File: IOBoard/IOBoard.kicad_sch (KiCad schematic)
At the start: 1 part, among them J1 Conn_02x20_Odd_Even

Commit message: complete schematic for usb hub
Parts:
- added C1, C2, C3: 10uF, symbol Device:C
- added J2, J3, J5: USB_A, symbol Connector:USB_A
- added J4, J6: USB_C_Receptacle_USB2.0_14P, symbol Connector:USB_C_Receptacle_USB2.0_14P
- added R1, R2, R3, R4: 5.1k, symbol Device:R
- added U1: ~, SL2.1A:SOP-16_L10.0-W3.9-P1.27-LS6.0-BL, symbol SL2.1A:SL2.1A
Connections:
- new net: C3.2, U1.13 (VDD33)
- new net: J4.A5 (CC1), R2.1
- new net: J4.A6 (D+), J4.B6 (D+), U1.4 (DP3)
- new net: J4.A7 (D-), J4.B7 (D-), U1.3 (DM3)
- new net: J4.B5 (CC2), R1.1
- new net: J6.A5 (CC1), R4.1
- new net: J3.2 (D-), U1.7 (DM1)
- new net: J3.3 (D+), U1.8 (DP1)
- new net: J6.A6 (D+), J6.B6 (D+), U1.2 (DP4)
- new net: J6.A7 (D-), J6.B7 (D-), U1.1 (DM4)
- new net: J6.B5 (CC2), R3.1
- new net: J2.3 (D+), U1.10 (DP)
- new net: C2.2, U1.14 (VDD18)
- new net: J5.2 (D-), U1.5 (DM2)
- new net: J5.3 (D+), U1.6 (DP2)
- new net: J2.2 (D-), U1.9 (DM)
- new net GND: C1.2, C2.1, C3.1, J2.4 (GND), J2.5 (Shield), J3.4 (GND), J3.5 (Shield), J4.A1 (GND), J4.A12 (GND), J4.B1 (GND), J4.B12 (GND), J4.S1 (SHIELD), J5.4 (GND), J5.5 (Shield), J6.A1 (GND), J6.A12 (GND), J6.B1 (GND), J6.B12 (GND), J6.S1 (SHIELD), R1.2, R2.2, R3.2, R4.2, U1.12 (GND), U1.16 (XIN)
- new net VCC: C1.1, J2.1 (VBUS), J3.1 (VBUS), J4.A4 (VBUS), J4.A9 (VBUS), J4.B4 (VBUS), J4.B9 (VBUS), J5.1 (VBUS), J6.A4 (VBUS), J6.A9 (VBUS), J6.B4 (VBUS), J6.B9 (VBUS), U1.11 (VDD5)
- no-connect marks 0 -> 1

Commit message: feat: complete IOBoard
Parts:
- removed J3, J5: USB_A, symbol Connector:USB_A
- added C4, C5, C6, C7: 10uF, Capacitor_SMD:C_0603_1608Metric, symbol Device:C
- added D1: D, Diode_SMD:D_SOD-323, symbol Device:D
- added J7: Conn_01x03, Connector_PinHeader_2.54mm:PinHeader_1x03_P2.54mm_Vertical, symbol Connector_Generic:Conn_01x03
- added J8: Conn_02x20_Odd_Even, Connector_PinHeader_2.54mm:PinHeader_2x20_P2.54mm_Vertical, symbol Connector_Generic:Conn_02x20_Odd_Even
- added USB1: ~, Components:USB-A-TH_AF-SS-JB17.6, symbol USB:AF SS-JB17.6
- C1, C2, C3: footprint (none) -> Capacitor_SMD:C_0603_1608Metric
- J2: footprint (none) -> Components:USB-A-TH_USB-231-ARY
- J4, J6: footprint (none) -> Components:USB-TYPE-C-SMD_TYPE-C-16P-QTWT
- R1, R2, R3, R4: footprint (none) -> Resistor_SMD:R_0603_1608Metric
- U1: footprint SL2.1A:SOP-16_L10.0-W3.9-P1.27-LS6.0-BL -> Components:SL2.1A
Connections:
- net GND: now also J1.14 (Pin_14), J1.20 (Pin_20), J1.25 (Pin_25), J1.30 (Pin_30), J1.34 (Pin_34), J1.39 (Pin_39), J1.6 (Pin_6), J1.9 (Pin_9), C4.2, C5.2, C6.1, C7.1, J7.3 (Pin_3), J8.14 (Pin_14), J8.20 (Pin_20), J8.25 (Pin_25), J8.30 (Pin_30), J8.34 (Pin_34), J8.39 (Pin_39), J8.6 (Pin_6), J8.9 (Pin_9), USB1.10 (SHELL), USB1.11 (SHELL), USB1.12 (SHELL), USB1.4 (GND), USB1.8 (GND), USB1.9 (SHELL)
- net VCC: now also J1.2 (Pin_2), J1.4 (Pin_4), C4.1, C5.1, C6.2, C7.2, D1.1 (K), J7.2 (Pin_2), J8.2 (Pin_2), J8.4 (Pin_4), USB1.1 (VCC), USB1.5 (VCC); no longer C1.1, J2.1 (VBUS)
- net at U1.7 (DM1): now also USB1.2 (D-)
- net at U1.8 (DP1): now also USB1.3 (D+)
- net +3.3V: now reaches J1.1 (Pin_1)
- net +3.3V: now also J1.17 (Pin_17), J8.1 (Pin_1), J8.17 (Pin_17)
- net GPIO_16: now reaches J1.10 (Pin_10)
- net GPIO_16: now also J8.10 (Pin_10)
- net GPIO_0: now reaches J1.11 (Pin_11)
- net GPIO_0: now also J8.11 (Pin_11)
- net GPIO_1: now reaches J1.12 (Pin_12)
- net GPIO_1: now also J8.12 (Pin_12)
- net GPIO_2: now reaches J1.13 (Pin_13)
- net GPIO_2: now also J8.13 (Pin_13)
- net GPIO_3: now reaches J1.15 (Pin_15)
- net GPIO_3: now also J8.15 (Pin_15)
- net GPIO_4: now reaches J1.16 (Pin_16)
- net GPIO_4: now also J8.16 (Pin_16)
- net GPIO_5: now reaches J1.18 (Pin_18)
- net GPIO_5: now also J8.18 (Pin_18)
- net GPIO_12: now reaches J1.19 (Pin_19)
- net GPIO_12: now also J8.19 (Pin_19)
- net GPIO_13: now reaches J1.21 (Pin_21)
- net GPIO_13: now also J8.21 (Pin_21)
- net GPIO_6: now reaches J1.22 (Pin_22)
- net GPIO_6: now also J8.22 (Pin_22)
- net GPIO_14: now reaches J1.23 (Pin_23)
- net GPIO_14: now also J8.23 (Pin_23)
- net GPIO_10: now reaches J1.24 (Pin_24)
- net GPIO_10: now also J8.24 (Pin_24)
- net GPIO_11: now reaches J1.26 (Pin_26)
- net GPIO_11: now also J8.26 (Pin_26)
- net GPIO_30: now reaches J1.27 (Pin_27)
- net GPIO_30: now also J8.27 (Pin_27)
- net GPIO_31: now reaches J1.28 (Pin_28)
- net GPIO_31: now also J8.28 (Pin_28)
- net GPIO_21: now reaches J1.29 (Pin_29)
- net GPIO_21: now also J8.29 (Pin_29)
- net GPIO_8: now reaches J1.3 (Pin_3)
- net GPIO_8: now also J8.3 (Pin_3)
- net GPIO_22: now reaches J1.31 (Pin_31)
- net GPIO_22: now also J8.31 (Pin_31)
- net GPIO_26: now reaches J1.32 (Pin_32)
- net GPIO_26: now also J7.1 (Pin_1), J8.32 (Pin_32)
- net GPIO_23: now reaches J1.33 (Pin_33)
- net GPIO_23: now also J8.33 (Pin_33)
- net GPIO_24: now reaches J1.35 (Pin_35)
- net GPIO_24: now also J8.35 (Pin_35)
- net GPIO_27: now reaches J1.36 (Pin_36)
- net GPIO_27: now also J8.36 (Pin_36)
- net GPIO_25: now reaches J1.37 (Pin_37)
- net GPIO_25: now also J8.37 (Pin_37)
- net GPIO_28: now reaches J1.38 (Pin_38)
- net GPIO_28: now also J8.38 (Pin_38)
- net GPIO_29: now reaches J1.40 (Pin_40)
- net GPIO_29: now also J8.40 (Pin_40)
- net GPIO_9: now reaches J1.5 (Pin_5)
- net GPIO_9: now also J8.5 (Pin_5)
- net GPIO_7: now reaches J1.7 (Pin_7)
- net GPIO_7: now also J8.7 (Pin_7)
- net GPIO_15: now reaches J1.8 (Pin_8)
- net GPIO_15: now also J8.8 (Pin_8)
- net at U1.5 (DM2): now also USB1.6 (D-)
- net at U1.6 (DP2): now also USB1.7 (D+)
- new net: C1.1, D1.2 (A), J2.1 (VBUS)
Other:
- note added: "Pinout Passthrough"
- moved on the sheet: J1, R2

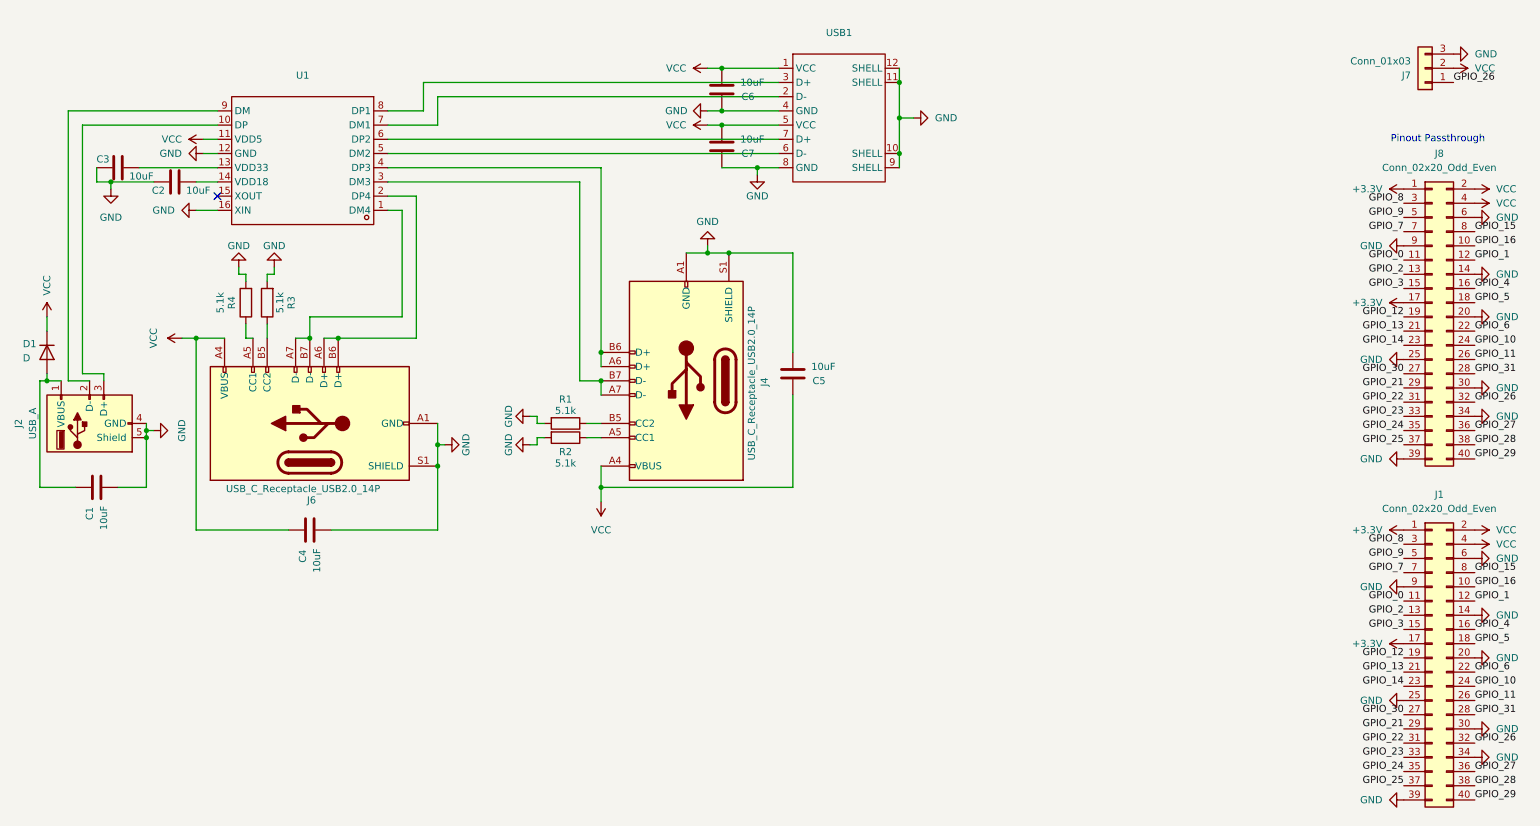
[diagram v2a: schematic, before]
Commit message: Update IOBoard usb c connectors
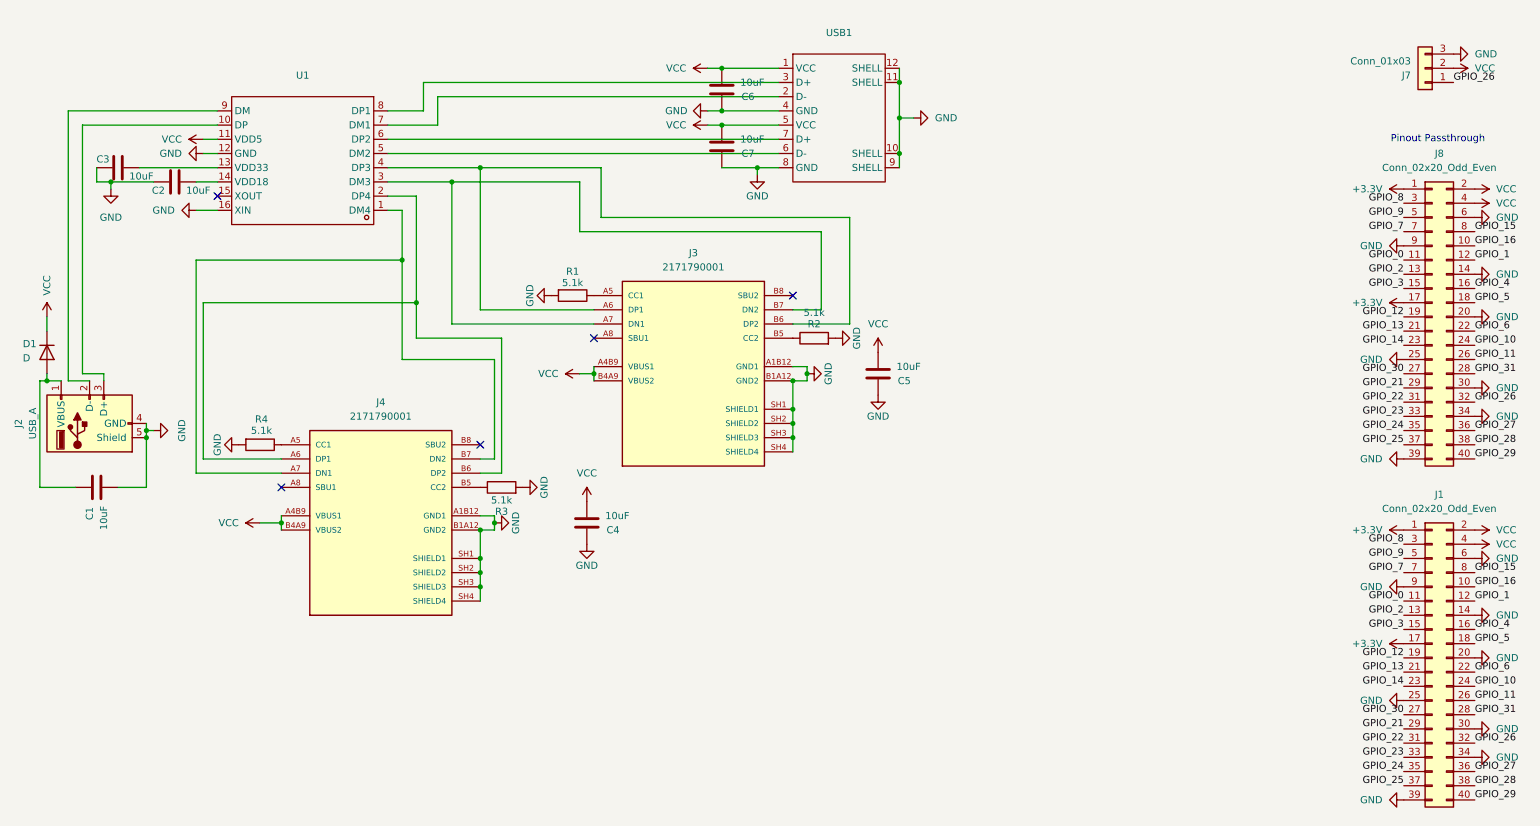
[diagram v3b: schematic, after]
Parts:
- removed J4, J6: USB_C_Receptacle_USB2.0_14P, Components:USB-TYPE-C-SMD_TYPE-C-16P-QTWT, symbol Connector:USB_C_Receptacle_USB2.0_14P
- added J3, J4: 2171790001, Components:MOLEX_2171790001, symbol USB C:2171790001
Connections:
- net GND: now also C4.1, C5.1, J3.A1B12 (GND1), J3.B1A12 (GND2), J3.SH1 (SHIELD1), J3.SH2 (SHIELD2), J3.SH3 (SHIELD3), J3.SH4 (SHIELD4), J4.A1B12 (GND1), J4.B1A12 (GND2), J4.SH1 (SHIELD1), J4.SH2 (SHIELD2), J4.SH3 (SHIELD3), J4.SH4 (SHIELD4); no longer C4.2, C5.2
- net VCC: now also C4.2, C5.2, J3.A4B9 (VBUS1), J3.B4A9 (VBUS2), J4.A4B9 (VBUS1), J4.B4A9 (VBUS2); no longer C4.1, C5.1
- net at R2.1: now also J3.B5 (CC2)
- net at U1.4 (DP3): now also J3.A6 (DP1), J3.B6 (DP2)
- net at U1.3 (DM3): now also J3.A7 (DN1), J3.B7 (DN2)
- net at R1.1: now also J3.A5 (CC1)
- net at R4.1: now also J4.A5 (CC1)
- net at U1.2 (DP4): now also J4.A6 (DP1), J4.B6 (DP2)
- net at U1.1 (DM4): now also J4.A7 (DN1), J4.B7 (DN2)
- net at R3.1: now also J4.B5 (CC2)
- no-connect marks 1 -> 5
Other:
- moved on the sheet: C4, C5, R1, R2, R3, R4
